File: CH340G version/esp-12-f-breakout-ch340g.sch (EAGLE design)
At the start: 21 parts, among them IC1 REG1117, Q1 12.000

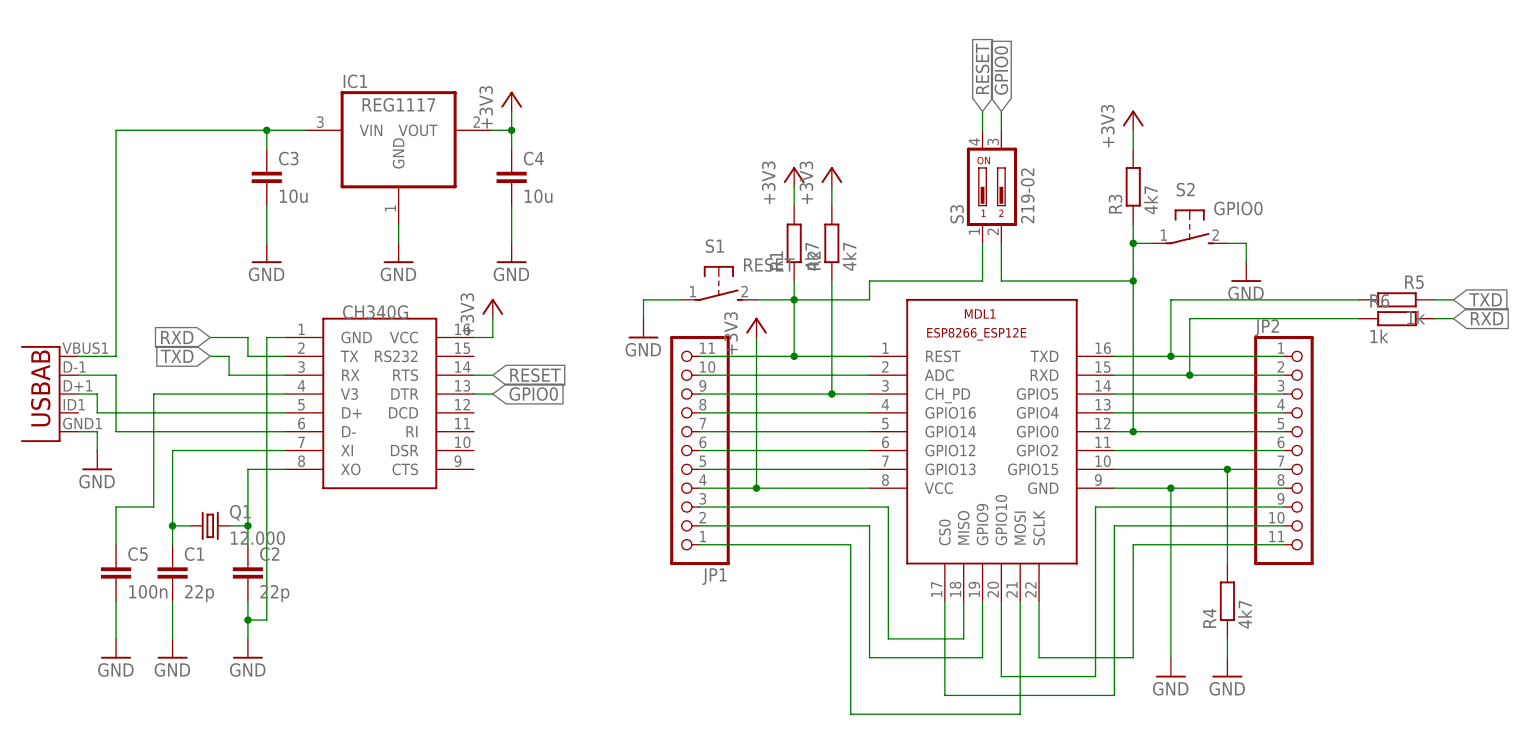
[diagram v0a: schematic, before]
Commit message: USB +5V pin added to pin headers
- Additional GND pin added
- Stabilizer layout rearranged
- Vias diameter slightly increased
- Drill-aid (0.4 mm) added
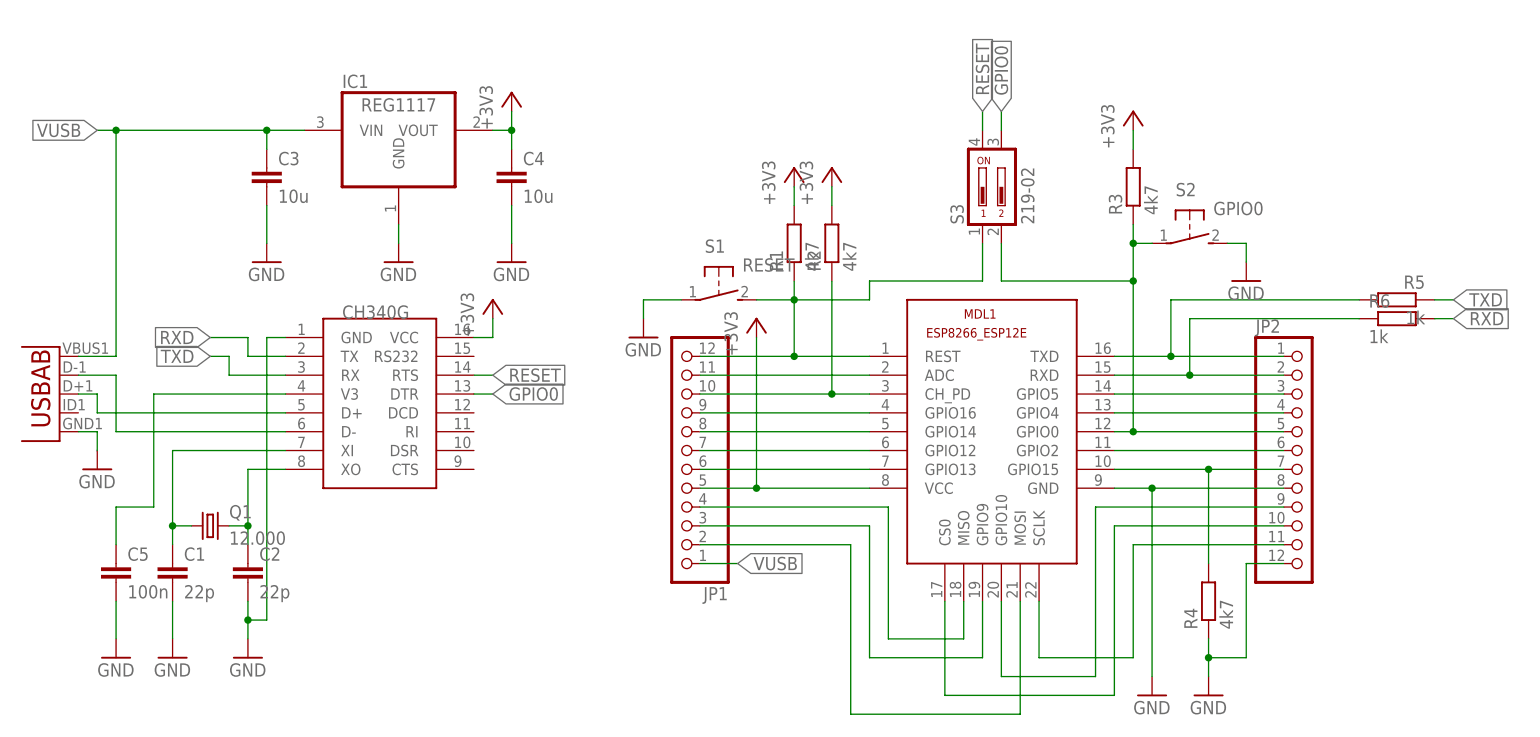
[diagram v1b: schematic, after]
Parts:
- JP1, JP2: device pinhead:PINHD-1X11 -> pinhead:PINHD-1X12
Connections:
- removed net N$27: C3.1, IC1.VIN, U2.VBUS
- new net VUSB: C3.1, IC1.VIN, JP1.1, U2.VBUS
- net +3V3: now also JP1.5; no longer JP1.4
- net GND: now also JP2.12
- net N$1: now also JP1.12; no longer JP1.11
- net N$11: now also JP1.3; no longer JP1.2
- net N$15: now also JP1.2; no longer JP1.1
- net N$2: now also JP1.11; no longer JP1.10
- net N$3: now also JP1.10; no longer JP1.9
- net N$4: now also JP1.9; no longer JP1.8
- net N$5: now also JP1.8; no longer JP1.7
- net N$6: now also JP1.7; no longer JP1.6
- net N$7: now also JP1.6; no longer JP1.5
- net N$8: now also JP1.4; no longer JP1.3
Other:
- moved on the sheet: R4
